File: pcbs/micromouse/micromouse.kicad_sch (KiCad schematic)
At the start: 28 parts, among them SW1 SW_SPDT, SW2 SW_Push, U1 AMS1117-5.0, U3 L7806

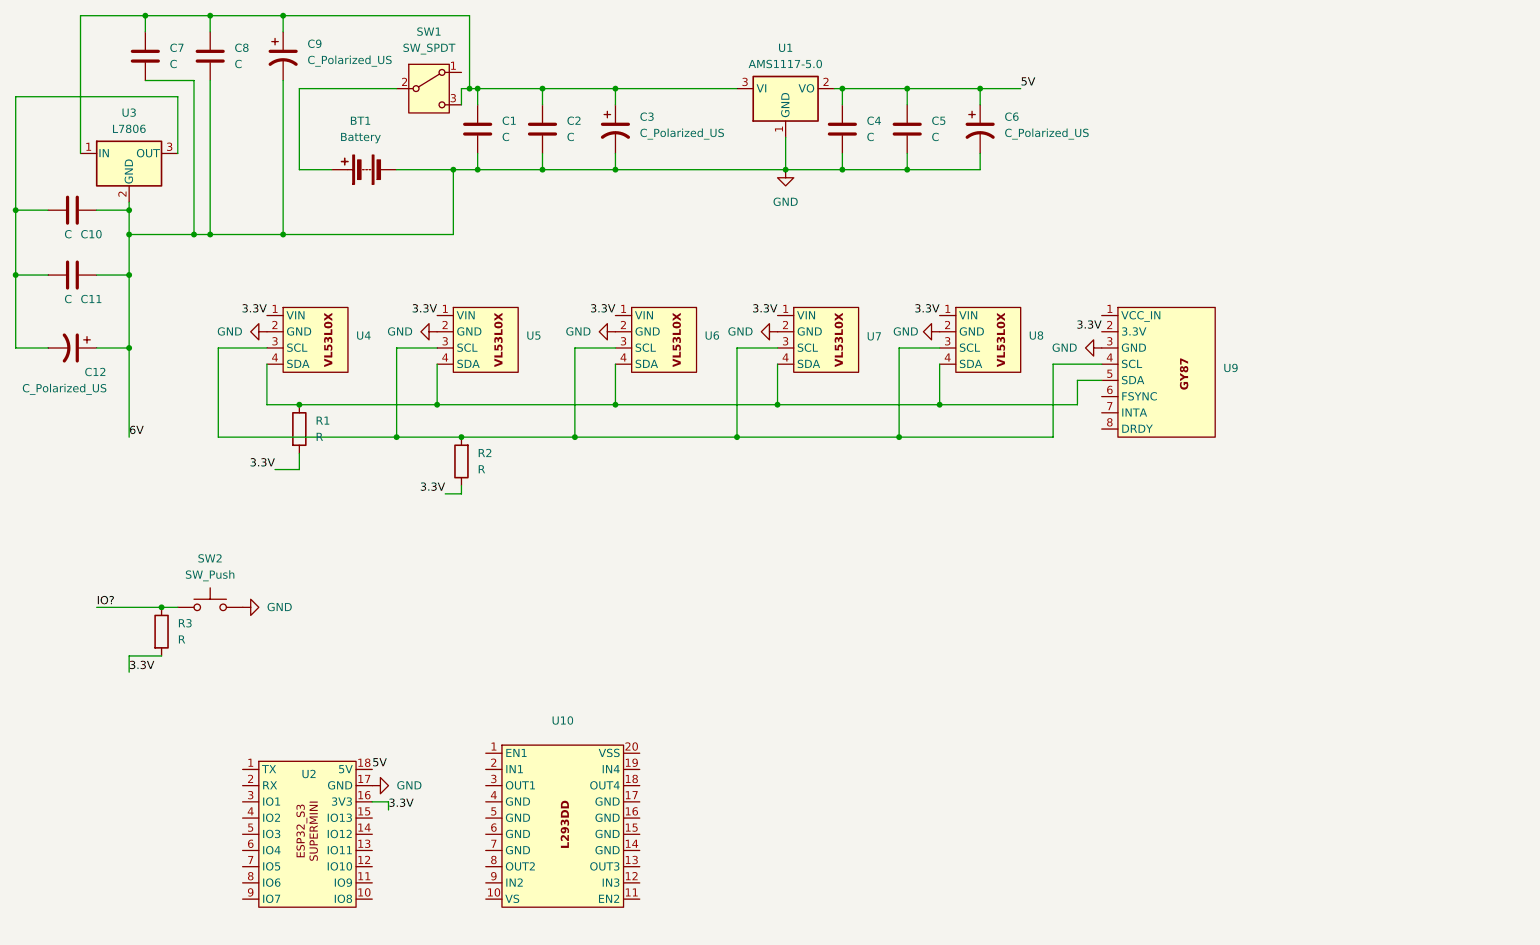
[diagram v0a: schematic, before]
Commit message: add motors and driver
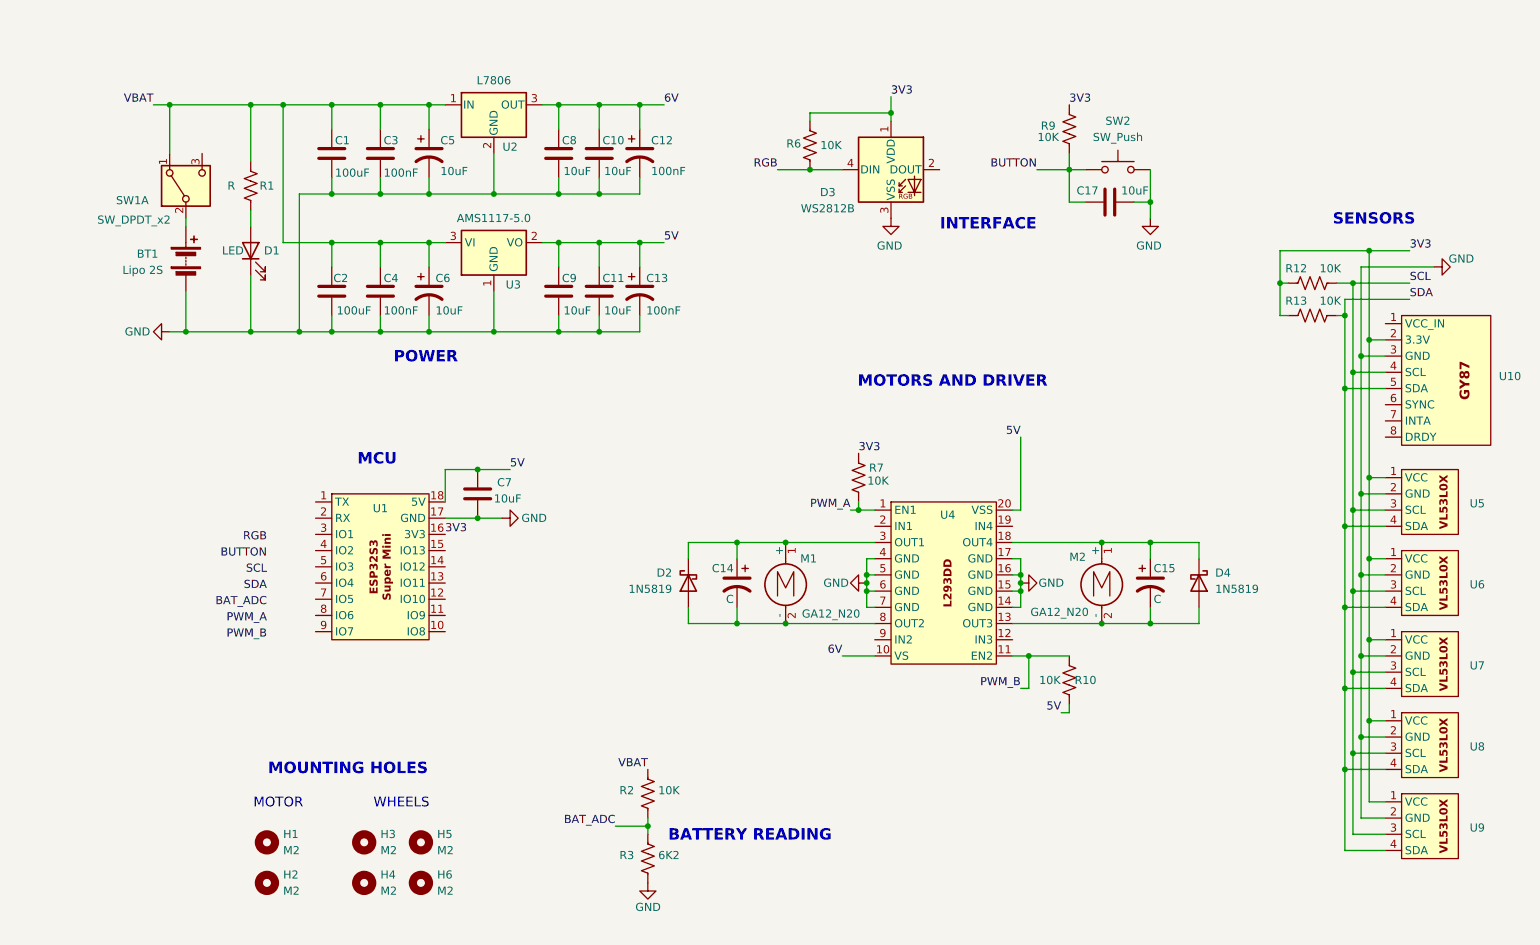
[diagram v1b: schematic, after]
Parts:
- removed C3, C9: C_Polarized_US, symbol Device:C_Polarized_US
- removed C5: C, symbol Device:C
- removed R1, R2, R3: R, symbol Device:R
- removed SW1: SW_SPDT, symbol Switch:SW_SPDT
- removed U1: AMS1117-5.0, Package_TO_SOT_SMD:SOT-223-3_TabPin2, symbol Regulator_Linear:AMS1117-5.0
- removed U10: ~, Package_SO:SOP-20_7.5x12.8mm_P1.27mm, symbol L293DD:L293DD
- removed U2: ~, Esp32_s3_supermini:Esp32_S3_Supermini, symbol esp32s3_supermini:Esp32_s3_supermini
- removed U3: L7806, Package_TO_SOT_THT:TO-220-3_Vertical, symbol Regulator_Linear:L7806
- removed U4, U5, U6, U7, U8: ~, VL53L0X_ToF_Sensor:VL53L0X ToF Sensor, symbol VL53L0X_ToF_Sensor_sym:VL53L0X_ToF_Sensor
- removed U9: ~, GY87:GY87, symbol GY87:GY87
- added C13: 100nF, symbol Device:C_Polarized_US
- added C14, C15: C, symbol Device:C_Polarized_US
- added C17, C9: 10uF, Capacitor_SMD:C_0805_2012Metric_Pad1.18x1.45mm_HandSolder, symbol Device:C
- added C3: 100nF, Capacitor_SMD:C_0805_2012Metric_Pad1.18x1.45mm_HandSolder, symbol Device:C
- added C5: 10uF, symbol Device:C_Polarized_US
- added D1: LED, symbol Device:LED
- added D2, D4: 1N5819, Diode_SMD:D_SOD-323F, symbol Diode:1N5819
- added D3: WS2812B, LED_SMD:LED_WS2812B_PLCC4_5.0x5.0mm_P3.2mm, symbol LED:WS2812B
- added H1, H2, H3, H4, H5, H6: M2, MountingHole:MountingHole_2.2mm_M2, symbol Mechanical:MountingHole
- added M1, M2: GA12_N20, N20_DC_Motor:N20_DC_Motor, symbol Motor:Motor_DC
- added R1: R, Resistor_SMD:R_0805_2012Metric_Pad1.20x1.40mm_HandSolder, symbol Device:R_US
- added R10, R12, R13, R2, R6, R7, R9: 10K, Resistor_SMD:R_0805_2012Metric_Pad1.20x1.40mm_HandSolder, symbol Device:R_US
- added R3: 6K2, Resistor_SMD:R_0805_2012Metric_Pad1.20x1.40mm_HandSolder, symbol Device:R_US
- added SW1: SW_DPDT_x2, SW_SS12D07VG4:SW_SS12D07VG4, symbol Switch:SW_DPDT_x2
- added U1: ~, ESP32_modules:esp32s3_super_mini, symbol ESP32_modules:esp32s3_super_mini
- added U10: ~, GY87:GY87, symbol Sensors_and_Modules:gy87
- added U2: L7806, Package_TO_SOT_THT:TO-220-3_Vertical, symbol Regulator_Linear:L7806
- added U3: AMS1117-5.0, Package_TO_SOT_SMD:SOT-223-3_TabPin2, symbol Regulator_Linear:AMS1117-5.0
- added U4: ~, Package_SO:SOP-20_7.5x12.8mm_P1.27mm, symbol External_ICs:L293DD
- added U5, U6, U7, U8, U9: ~, VL53L0X:VL53L0X_vertical, symbol VL53L0X:VL53L0X
- BT1: value Battery -> Lipo 2S
- C1, C2: value C -> 100uF; footprint (none) -> Capacitor_SMD:C_0805_2012Metric_Pad1.18x1.45mm_HandSolder
- C10, C11, C7, C8: value C -> 10uF; footprint (none) -> Capacitor_SMD:C_0805_2012Metric_Pad1.18x1.45mm_HandSolder
- C12: value C_Polarized_US -> 100nF
- C4: value C -> 100nF; footprint (none) -> Capacitor_SMD:C_0805_2012Metric_Pad1.18x1.45mm_HandSolder
- C6: value C_Polarized_US -> 10uF
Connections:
- net 5V: now also C11.1, C7.1, C13.1, C9.1, R10.2, U1.18 (5V), U3.2 (VO), U4.20 (VSS); no longer C4.1, C6.1
- net GND: now also C10.2, C11.2, C12.2, C13.2, C17.2, C3.2, C5.2, C9.2, D1.1 (K), D3.3 (VSS), R3.1, U1.17 (GND), U10.3 (GND), U2.2 (GND), U3.1 (GND), U4.14 (GND), U4.15 (GND), U4.16 (GND), U4.17 (GND), U4.4 (GND), U4.5 (GND), U4.6 (GND), U4.7 (GND), U5.2 (GND), U6.2 (GND), U7.2 (GND), U8.2 (GND), U9.2 (GND); no longer C10.1, C11.1, C12.1
- net VBAT: now reaches C1.1, C2.1
- net VBAT: now also C4.1, C6.1, C3.1, C5.1, R1.1, R2.2, SW1.1 (A), U2.1 (IN), U3.3 (VI); no longer C7.1, C8.1
- net at BT1.1 (+): now also SW1.2 (B)
- net IO? renamed BUTTON
- net BUTTON: now also C17.1, R9.1
- new net: C14.1, D2.1 (K), M1.1 (+), U4.3 (OUT1)
- new net: C14.2, D2.2 (A), M1.2 (-), U4.8 (OUT2)
- new net: D1.2 (A), R1.2
- new net: C15.1, D4.1 (K), M2.1 (+), U4.18 (OUT4)
- new net: C15.2, D4.2 (A), M2.2 (-), U4.13 (OUT3)
- new net 3V3: D3.1 (VDD), R12.1, R13.1, R6.2, R7.2, R9.2, U1.16 (3V3), U10.2 (3.3V), U5.1 (VCC), U6.1 (VCC), U7.1 (VCC), U8.1 (VCC), U9.1 (VCC)
- new net 6V: C10.1, C12.1, C8.1, U2.3 (OUT), U4.10 (VS)
- new net BAT_ADC: R2.1, R3.2
- new net PWM_A: R7.1, U4.1 (EN1)
- new net PWM_B: R10.1, U4.11 (EN2)
- new net RGB: D3.4 (DIN), R6.1
- new net SCL: R12.2, U10.4 (SCL), U5.3 (SCL), U6.3 (SCL), U7.3 (SCL), U8.3 (SCL), U9.3 (SCL)
- new net SDA: R13.2, U10.5 (SDA), U5.4 (SDA), U6.4 (SDA), U7.4 (SDA), U8.4 (SDA), U9.4 (SDA)
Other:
- note added: "BATTERY READING"
- note added: "INTERFACE"
- note added: "MCU"
- note added: "MOTOR"
- note added: "MOTORS AND DRIVER"
- note added: "MOUNTING HOLES"
- note added: "POWER"
- note added: "SENSORS"
- note added: "WHEELS"
- title: (none) -> Neural Network-based Micromouse

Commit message: schematic_done
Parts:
- removed H1, H2: M2, MountingHole:MountingHole_2.2mm_M2, symbol Mechanical:MountingHole
- added R11, R4, R5, R8: 10K, Resistor_SMD:R_0805_2012Metric_Pad1.20x1.40mm_HandSolder, symbol Device:R_US
- BT1: footprint (none) -> XH_2p54:2P_male
- C12, C13, C14, C15, C5, C6: footprint (none) -> Capacitor_THT:CP_Radial_D5.0mm_P2.00mm
- D1: footprint (none) -> LED_SMD:LED_0805_2012Metric_Pad1.15x1.40mm_HandSolder
- SW2: footprint (none) -> Button_Switch_SMD:SW_SPST_CK_RS282G05A3
- U5, U6, U7, U8, U9: footprint VL53L0X:VL53L0X_vertical -> VL53L0X_ToF_Sensor:VL53L0X ToF Sensor
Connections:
- net 5V: now also R4.1, R5.1
- net GND: now also R11.1, R8.1
- net at U4.12 (IN3): now also R11.2
- net at U4.19 (IN4): now also R5.2
- net at U4.2 (IN1): now also R4.2
- net at U4.9 (IN2): now also R8.2
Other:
- note added: "WHEEL MOUNTING HOLES"
- note removed: "MOTOR"
- note removed: "MOUNTING HOLES"
- note removed: "WHEELS"
- moved on the sheet: H3, H4, H5, H6

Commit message: 100% done
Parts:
- added C16: 10uF, Capacitor_SMD:C_0805_2012Metric_Pad1.18x1.45mm_HandSolder, symbol Device:C
- added H1, H2, H7, H8: M2, MountingHole:MountingHole_2.2mm_M2, symbol Mechanical:MountingHole
- M1: renamed from M2; footprint N20_DC_Motor:N20_DC_Motor -> XH_2p54:2P_male
- M2: renamed from M1; footprint N20_DC_Motor:N20_DC_Motor -> XH_2p54:2P_male
- U5, U6, U7, U8, U9: footprint VL53L0X_ToF_Sensor:VL53L0X ToF Sensor -> VL53L0X:VL53L0X_vertical
- renumbered C15 to C14, C14 to C15, D4 to D2, D2 to D4
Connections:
- net 3V3: now also R10.2
- net 5V: no longer R10.2
- net BAT_ADC: now also U1.12 (IO10), C16.1
- net BUTTON: now also U1.3 (IO1)
- net GND: now also C16.2
- net PWM_A: now also U1.7 (IO5)
- net PWM_B: now also U1.6 (IO4)
- net RGB: now also U1.15 (IO13)
- net SCL: now also U1.4 (IO2)
- net SDA: now also U1.5 (IO3)
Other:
- note added: "MOUNTNG HOLES"
- note added: "Motor Brackets"
- note added: "Wheels"
- note removed: "WHEEL MOUNTING HOLES"
- moved on the sheet: D4, H3, H4, H5, H6

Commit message: pcb gerbers done
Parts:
- C12, C13: value 100nF -> 470nF
- C14, C15: value C -> 0.1uF
- C8, C9: value 10uF -> 0.1uF
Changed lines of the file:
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@@
 	(wire
 		(pts
-			(xy 173.99 82.55) (xy 173.99 93.98)
+			(xy 173.99 87.63) (xy 173.99 93.98)
 		)
 		(stroke
@@
 	)
 	(label "5V"
-		(at 173.99 82.55 180)
+		(at 173.99 87.63 180)
 		(fields_autoplaced yes)
 		(effects
@@
 			)
 		)
-		(property "Value" "100nF"
+		(property "Value" "470nF"
 			(at 116.078 40.894 0)
 			(effects
@@
 			)
 		)
-		(property "Value" "10uF"
+		(property "Value" "0.1uF"
 			(at 102.362 62.738 0)
 			(effects
@@
 			)
 		)
-		(property "Value" "C"
+		(property "Value" "0.1uF"
 			(at 194.818 107.95 0)
 			(effects
@@
 			)
 		)
-		(property "Value" "100nF"
+		(property "Value" "470nF"
 			(at 115.316 62.738 0)
 			(effects
@@
 		(dnp no)
 		(property "Reference" "R10"
-			(at 184.15 120.65 0)
+			(at 184.404 120.65 0)
 			(effects
 				(font
@@
 			)
 		)
-		(property "Value" "10uF"
+		(property "Value" "0.1uF"
 			(at 102.362 40.894 0)
 			(effects
@@
 			)
 		)
-		(property "Value" "C"
+		(property "Value" "0.1uF"
 			(at 129.032 107.95 0)
 			(effects
